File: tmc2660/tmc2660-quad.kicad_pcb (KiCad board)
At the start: 4 copper layers, 26.7 x 31.1 mm, 16 parts, among them P3 Motor, U1 TMC2660

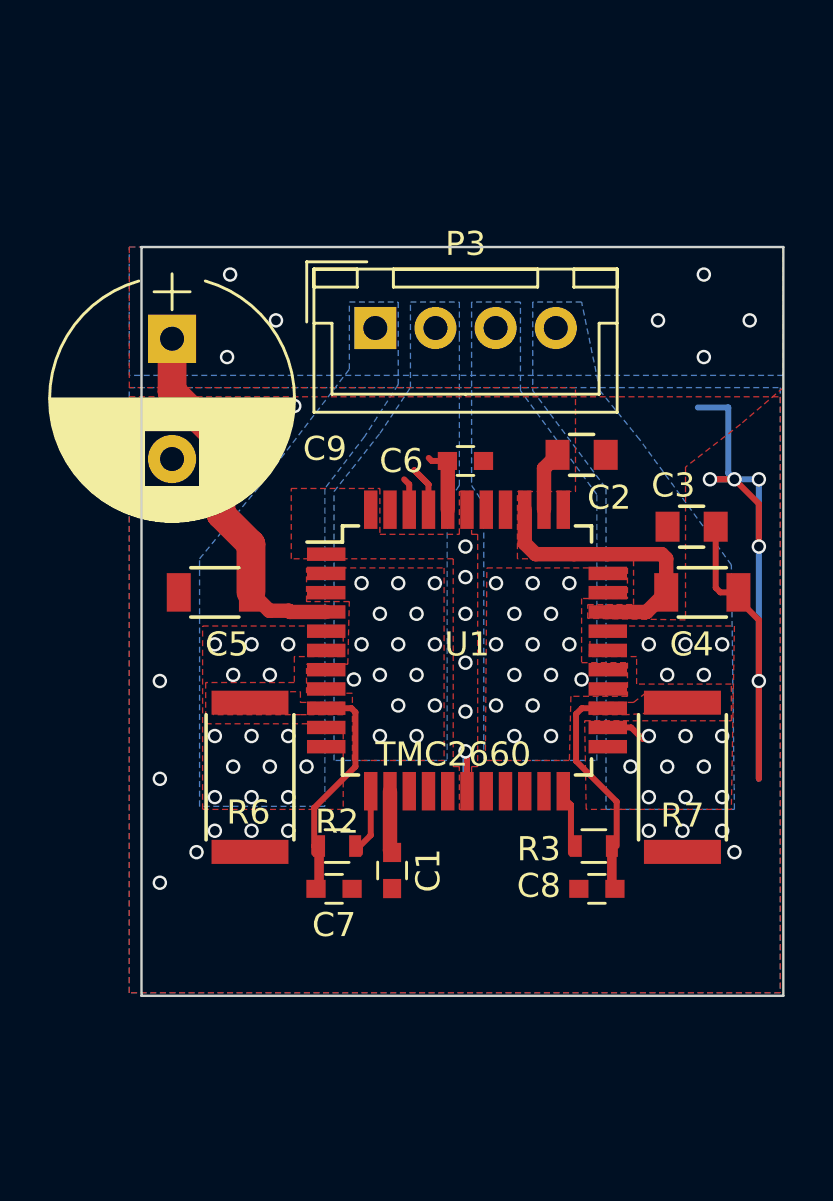
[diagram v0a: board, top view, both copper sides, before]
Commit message: Arrange ceramic VMOT caps more symmetrically.
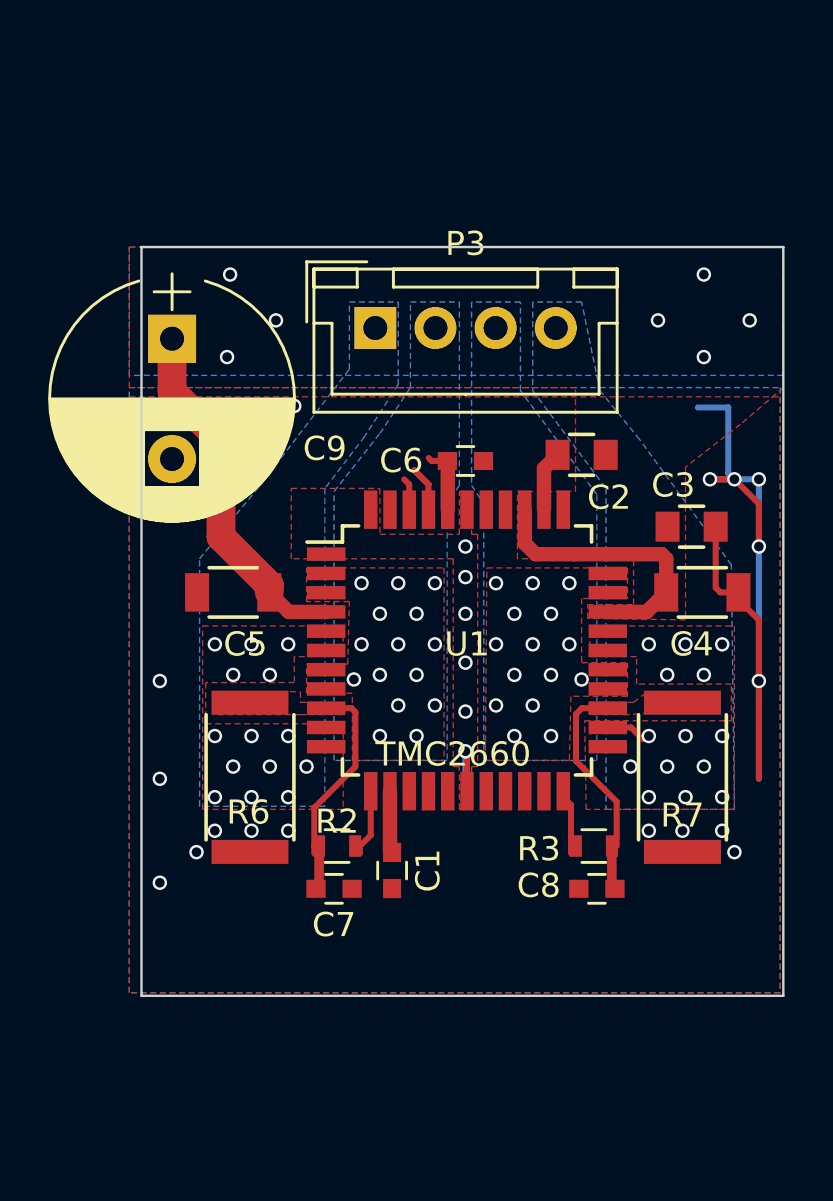
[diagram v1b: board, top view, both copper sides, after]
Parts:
- moved C5 0.76 mm to (120.1, 51.9)
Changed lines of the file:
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@@
   (thickness 1.6)
   (drawings 6)
-  (tracks 173)
+  (tracks 171)
   (zones 0)
   (modules 16)
@@
   )
   (module Capacitors_SMD:C_1206 (layer F.Cu)
-    (at 119.38 51.943 180)
+    (at 120.142 51.943 180)
     (descr "Capacitor SMD 1206, reflow soldering, AVX (see smccp.pdf)")
     (tags "capacitor 1206")
@@
   (segment (start 126.6575 60.206) (end 126.6575 62.6615) (width 0.6) (layer F.Cu) (net 2))
   (segment (start 126.6575 62.6615) (end 126.746 62.75) (width 0.6) (layer F.Cu) (net 2))
+  (segment (start 121.642 51.943) (end 122.455 52.756) (width 0.6) (layer F.Cu) (net 3))
+  (segment (start 122.455 52.756) (end 124.0075 52.756) (width 0.6) (layer F.Cu) (net 3))
+  (segment (start 117.602 41.402) (end 117.602 43.602) (width 1.2) (layer F.Cu) (net 3))
+  (segment (start 117.602 43.602) (end 119.634 45.634) (width 1.2) (layer F.Cu) (net 3))
+  (segment (start 119.634 45.634) (end 119.634 49.635) (width 1.2) (layer F.Cu) (net 3))
+  (segment (start 119.634 49.635) (end 121.642 51.643) (width 1.2) (layer F.Cu) (net 3))
+  (segment (start 121.642 51.643) (end 121.642 51.943) (width 1.2) (layer F.Cu) (net 3))
   (via (at 141.605 40.64) (size 0.6) (drill 0.4) (layers F.Cu B.Cu) (net 3))
   (via (at 139.7 42.164) (size 0.6) (drill 0.4) (layers F.Cu B.Cu) (net 3))
@@
   (via (at 119.888 42.164) (size 0.6) (drill 0.4) (layers F.Cu B.Cu) (net 3))
   (via (at 120.015 38.735) (size 0.6) (drill 0.4) (layers F.Cu B.Cu) (net 3))
-  (segment (start 121.642 52.705) (end 122.453 52.705) (width 0.6) (layer F.Cu) (net 3))
-  (segment (start 122.453 52.705) (end 122.504 52.756) (width 0.6) (layer F.Cu) (net 3))
-  (segment (start 120.88 51.943) (end 121.642 52.705) (width 0.6) (layer F.Cu) (net 3))
-  (segment (start 119.634 45.634) (end 119.634 48.697) (width 1.2) (layer F.Cu) (net 3))
-  (segment (start 119.634 48.697) (end 120.88 49.943) (width 1.2) (layer F.Cu) (net 3))
-  (segment (start 120.88 49.943) (end 120.88 51.943) (width 1.2) (layer F.Cu) (net 3))
-  (segment (start 117.602 41.402) (end 117.602 43.602) (width 1.2) (layer F.Cu) (net 3))
-  (segment (start 117.602 43.602) (end 119.634 45.634) (width 1.2) (layer F.Cu) (net 3))
   (segment (start 138.1365 51.943) (end 137.3235 52.756) (width 0.6) (layer F.Cu) (net 3))
   (segment (start 137.3235 52.756) (end 135.7075 52.756) (width 0.6) (layer F.Cu) (net 3))
@@
   (segment (start 132.7075 50.356) (end 134.3075 50.356) (width 0.6) (layer F.Cu) (net 3))
   (segment (start 134.3075 50.356) (end 135.7075 50.356) (width 0.6) (layer F.Cu) (net 3))
-  (segment (start 122.504 52.756) (end 124.0075 52.756) (width 0.6) (layer F.Cu) (net 3))
   (segment (start 133.62 46.228) (end 133.0575 46.7905) (width 0.6) (layer F.Cu) (net 4))
   (segment (start 133.0575 46.7905) (end 133.0575 48.506) (width 0.6) (layer F.Cu) (net 4))
@@
     (polygon
       (pts
-        (xy 135.001 53.34) (xy 140.97 53.34) (xy 140.843 60.96) (xy 134.8105 60.96) (xy 134.747 57.277)
+        (xy 135.001 53.34) (xy 140.97 53.34) (xy 140.97 60.96) (xy 134.8105 60.96) (xy 134.747 57.277)
         (xy 140.843 57.277) (xy 140.843 55.753) (xy 136.906 55.753) (xy 136.906 54.61) (xy 134.9375 54.61)
       )

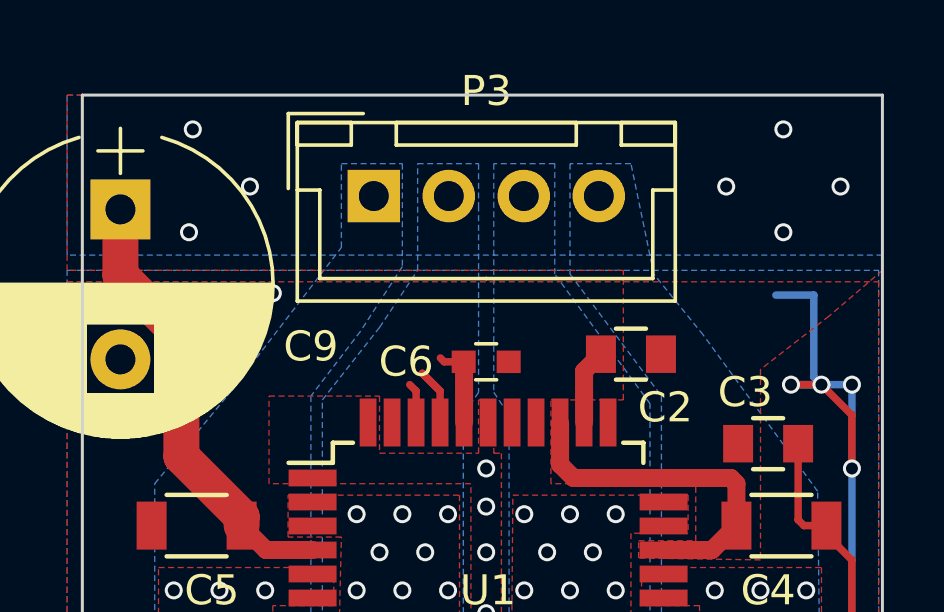
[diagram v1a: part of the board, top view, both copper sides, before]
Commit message: Add a VCC connecting bar.
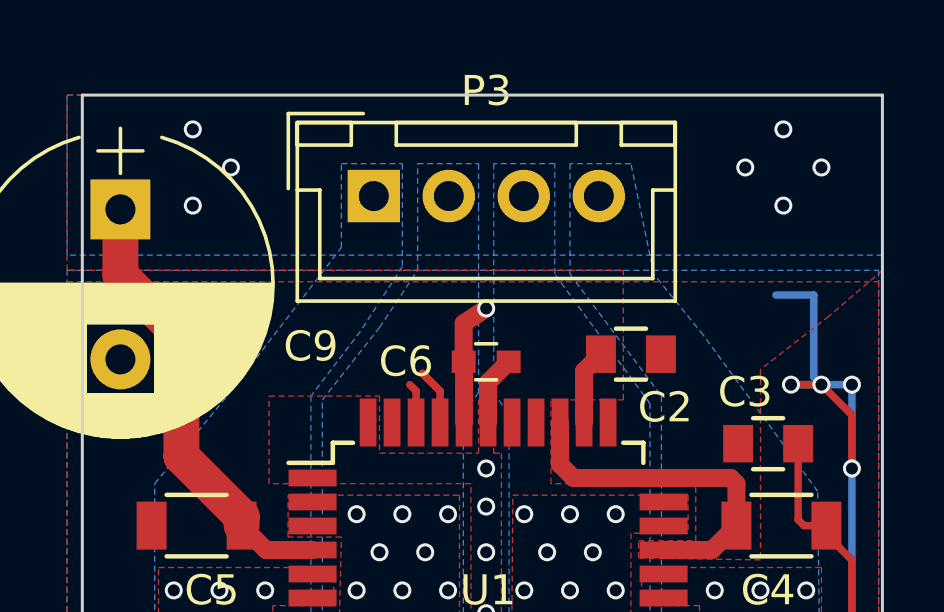
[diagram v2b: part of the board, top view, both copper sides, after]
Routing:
- net VCC: track 2.86 -> 5.99 mm, vias 0 -> 1
- net GND: track 37.4 -> 39.7 mm, vias 31 -> 28
- added copper zone on In2.Cu, net VCC
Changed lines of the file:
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@@
   (thickness 1.6)
   (drawings 6)
-  (tracks 171)
+  (tracks 172)
   (zones 0)
   (modules 16)
@@
 )
 (setup
-  (last_trace_width 0.25)
+  (last_trace_width 0.6)
   (user_trace_width 0.4)
   (user_trace_width 0.6)
@@
   (user_trace_width 1.2)
   (trace_clearance 0.127)
-  (zone_clearance 0.5)
+  (zone_clearance 0.254)
   (zone_45_only no)
   (trace_min 0.2)
@@
   (gr_line (start 143.002 37.592) (end 143.002 68.707) (layer Edge.Cuts) (width 0.1))
   (gr_line (start 116.332 37.592) (end 143.002 37.592) (layer Edge.Cuts) (width 0.1))
+  (segment (start 129.8575 48.506) (end 129.8575 47.1685) (width 0.6) (layer F.Cu) (net 1))
+  (segment (start 129.8575 47.1685) (end 130.544 46.482) (width 0.6) (layer F.Cu) (net 1))
   (via (at 116.967 44.704) (size 0.6) (drill 0.4) (layers F.Cu B.Cu) (net 1))
   (via (at 116.967 48.514) (size 0.6) (drill 0.4) (layers F.Cu B.Cu) (net 1))
   (via (at 118.237 48.514) (size 0.6) (drill 0.4) (layers F.Cu B.Cu) (net 1))
-  (via (at 120.904 45.339) (size 0.6) (drill 0.4) (layers F.Cu B.Cu) (net 1))
-  (via (at 121.412 44.196) (size 0.6) (drill 0.4) (layers F.Cu B.Cu) (net 1))
-  (via (at 121.158 46.355) (size 0.6) (drill 0.4) (layers F.Cu B.Cu) (net 1))
-  (via (at 121.92 45.339) (size 0.6) (drill 0.4) (layers F.Cu B.Cu) (net 1))
-  (via (at 122.682 44.196) (size 0.6) (drill 0.4) (layers F.Cu B.Cu) (net 1))
-  (via (at 120.142 44.196) (size 0.6) (drill 0.4) (layers F.Cu B.Cu) (net 1))
+  (via (at 121.285 45.339) (size 0.6) (drill 0.4) (layers F.Cu B.Cu) (net 1))
+  (via (at 122.047 44.45) (size 0.6) (drill 0.4) (layers F.Cu B.Cu) (net 1))
+  (via (at 120.523 44.45) (size 0.6) (drill 0.4) (layers F.Cu B.Cu) (net 1))
   (via (at 117.094 55.626) (size 0.6) (drill 0.4) (layers F.Cu B.Cu) (net 1))
   (via (at 140.97 62.738) (size 0.6) (drill 0.4) (layers F.Cu B.Cu) (net 1))
@@
   (segment (start 119.634 49.635) (end 121.642 51.643) (width 1.2) (layer F.Cu) (net 3))
   (segment (start 121.642 51.643) (end 121.642 51.943) (width 1.2) (layer F.Cu) (net 3))
-  (via (at 141.605 40.64) (size 0.6) (drill 0.4) (layers F.Cu B.Cu) (net 3))
-  (via (at 139.7 42.164) (size 0.6) (drill 0.4) (layers F.Cu B.Cu) (net 3))
+  (via (at 140.97 40.005) (size 0.6) (drill 0.4) (layers F.Cu B.Cu) (net 3))
+  (via (at 139.7 41.275) (size 0.6) (drill 0.4) (layers F.Cu B.Cu) (net 3))
   (via (at 139.7 38.735) (size 0.6) (drill 0.4) (layers F.Cu B.Cu) (net 3))
-  (via (at 137.795 40.64) (size 0.6) (drill 0.4) (layers F.Cu B.Cu) (net 3))
-  (via (at 121.92 40.64) (size 0.6) (drill 0.4) (layers F.Cu B.Cu) (net 3))
-  (via (at 119.888 42.164) (size 0.6) (drill 0.4) (layers F.Cu B.Cu) (net 3))
+  (via (at 138.43 40.005) (size 0.6) (drill 0.4) (layers F.Cu B.Cu) (net 3))
+  (via (at 121.285 40.005) (size 0.6) (drill 0.4) (layers F.Cu B.Cu) (net 3))
+  (via (at 120.015 41.275) (size 0.6) (drill 0.4) (layers F.Cu B.Cu) (net 3))
   (via (at 120.015 38.735) (size 0.6) (drill 0.4) (layers F.Cu B.Cu) (net 3))
   (segment (start 138.1365 51.943) (end 137.3235 52.756) (width 0.6) (layer F.Cu) (net 3))
@@
   (segment (start 135.878 62.484) (end 135.878 64.135) (width 0.4) (layer F.Cu) (net 10))
   (segment (start 135.878 64.135) (end 136.005 64.262) (width 0.4) (layer F.Cu) (net 10))
-  (segment (start 129.044 46.482) (end 128.394 46.482) (width 0.25) (layer F.Cu) (net 13))
-  (segment (start 128.394 46.482) (end 128.267 46.355) (width 0.25) (layer F.Cu) (net 13))
+  (via (at 129.794 44.704) (size 0.6) (drill 0.4) (layers F.Cu B.Cu) (net 13))
+  (segment (start 129.794 44.704) (end 129.044 45.2) (width 0.6) (layer F.Cu) (net 13))
+  (segment (start 129.794 44.704) (end 129.794 42.926) (width 0.6) (layer In2.Cu) (net 13))
+  (segment (start 129.044 45.2) (end 129.044 46.482) (width 0.6) (layer F.Cu) (net 13))
   (segment (start 129.0575 48.506) (end 129.0575 46.4955) (width 0.6) (layer F.Cu) (net 13))
   (segment (start 129.0575 46.4955) (end 129.044 46.482) (width 0.6) (layer F.Cu) (net 13))
@@
     (connect_pads yes (clearance 0.254))
     (min_thickness 0.254)
-    (fill yes (arc_segments 16) (thermal_gap 0.508) (thermal_bridge_width 0.508))
+    (fill yes (arc_segments 16) (thermal_gap 0.3) (thermal_bridge_width 0.508))
     (polygon
       (pts
@@
   )
   (zone (net 1) (net_name GND) (layer B.Cu) (hatch edge 0.508)
-    (connect_pads yes (clearance 0.254))
+    (connect_pads thru_hole_only (clearance 0.254))
     (min_thickness 0.254)
     (fill yes (arc_segments 16) (thermal_gap 0.508) (thermal_bridge_width 0.508))
@@
     (polygon
       (pts
-        (xy 115.824 37.592) (xy 143.002 37.592) (xy 143.002 43.18) (xy 115.824 43.18)
+        (xy 115.824 37.592) (xy 143.002 37.592) (xy 143.002 42.418) (xy 115.824 42.418)
       )
     )
@@
       )
     )
+  )
+  (zone (net 13) (net_name VCC) (layer In2.Cu) (hatch edge 0.508)
+    (priority 2)
+    (connect_pads yes (clearance 0.5))
+    (min_thickness 0.254)
+    (fill yes (arc_segments 16) (thermal_gap 0.508) (thermal_bridge_width 0.508))
+    (polygon
+      (pts
+        (xy 115.697 42.545) (xy 142.875 42.545) (xy 142.875 43.561) (xy 115.697 43.561)
+      )
+    )

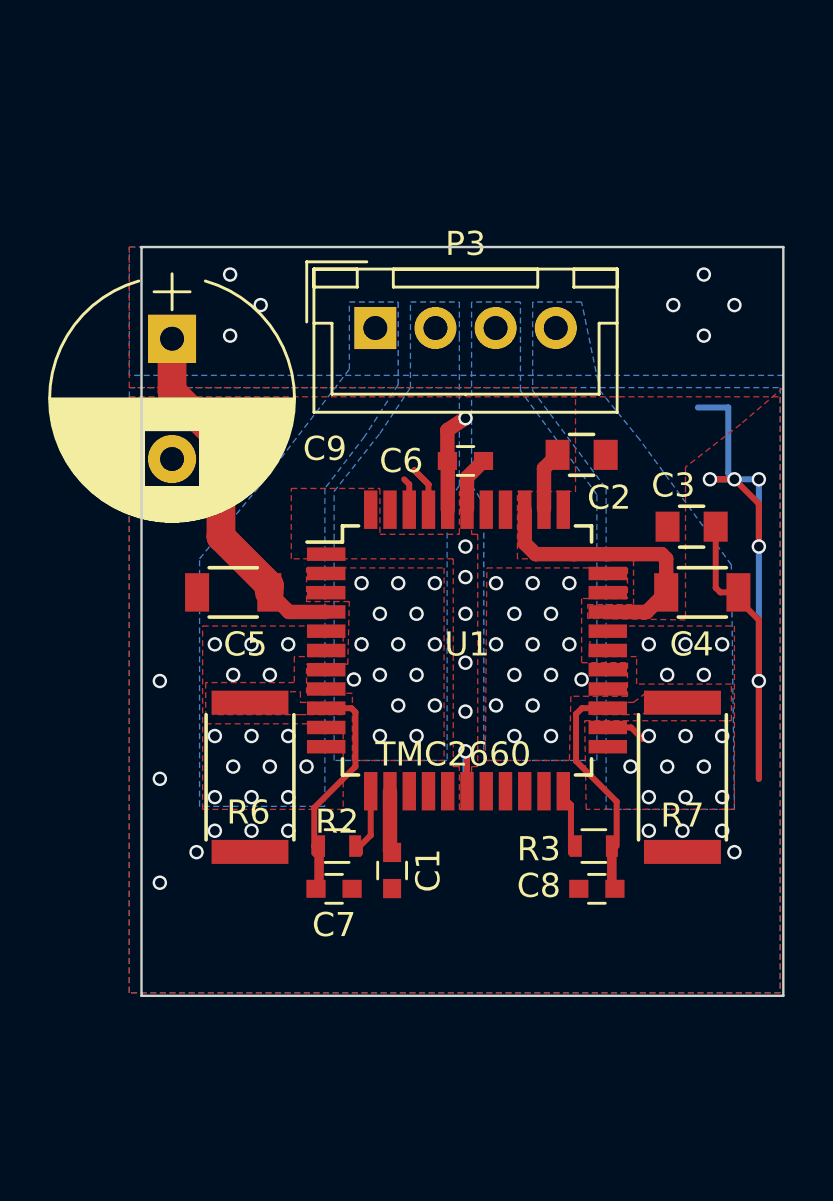
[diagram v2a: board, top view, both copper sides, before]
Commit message: Wire up SPI in signal layer; prepare Step/Dir.
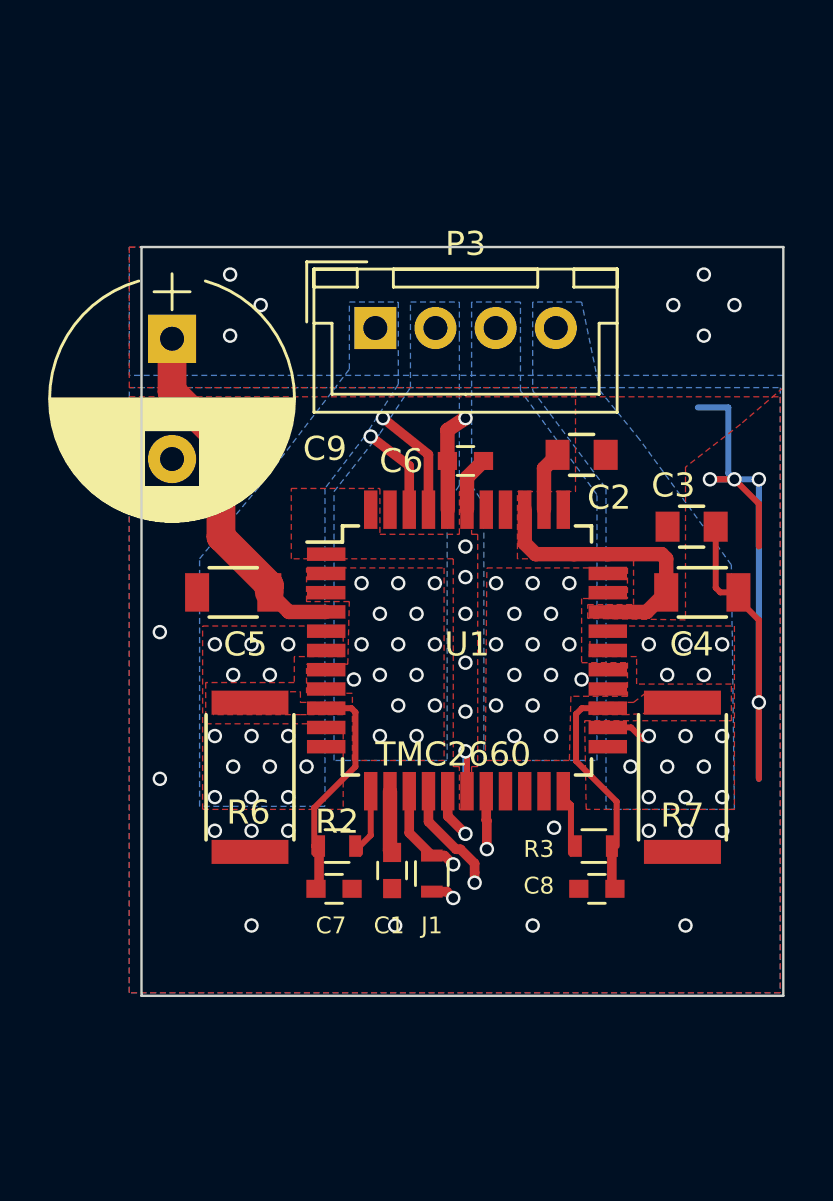
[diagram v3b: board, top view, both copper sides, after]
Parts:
- added J1: 0R, Resistors_SMD:R_0603, F.Cu at (128.4, 63.6)
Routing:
- net /CS_1: track 0.00 -> 30.5 mm, vias 0 -> 1
- net /SCLK_1: track 0.00 -> 30.0 mm, vias 0 -> 1
- net GLOBAL_MISO: track 0.00 -> 28.3 mm, vias 0 -> 1
- net /MOSI_1: track 0.00 -> 19.4 mm, vias 0 -> 1
- net /MISO_1: track 0.00 -> 18.5 mm, vias 0 -> 1
- net /STEP_1: track 1.35 -> 3.83 mm, vias 0 -> 1
- net /DIR_1: track 2.72 -> 4.71 mm, vias 0 -> 1
- net GND: vias 28 -> 29
- added copper zone on In1.Cu, net GND
